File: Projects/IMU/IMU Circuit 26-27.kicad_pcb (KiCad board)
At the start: 2 copper layers, 32.1 x 33.1 mm, 13 parts, among them U1 TJA1050DRG, U2 MCP2515-I, U3 TM171, X1 8MHz

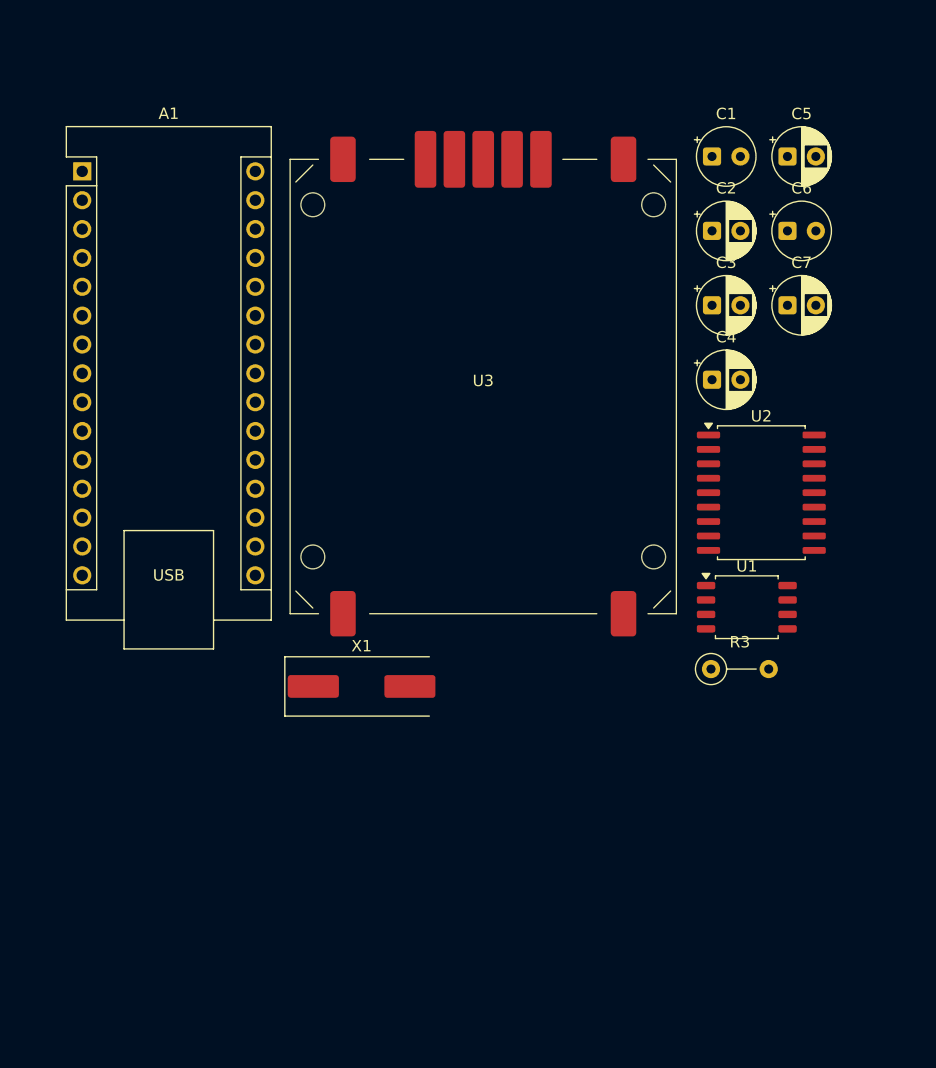
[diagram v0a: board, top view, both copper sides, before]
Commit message: the pcb update
(mostly) done routing, fill areas, and silkscreens
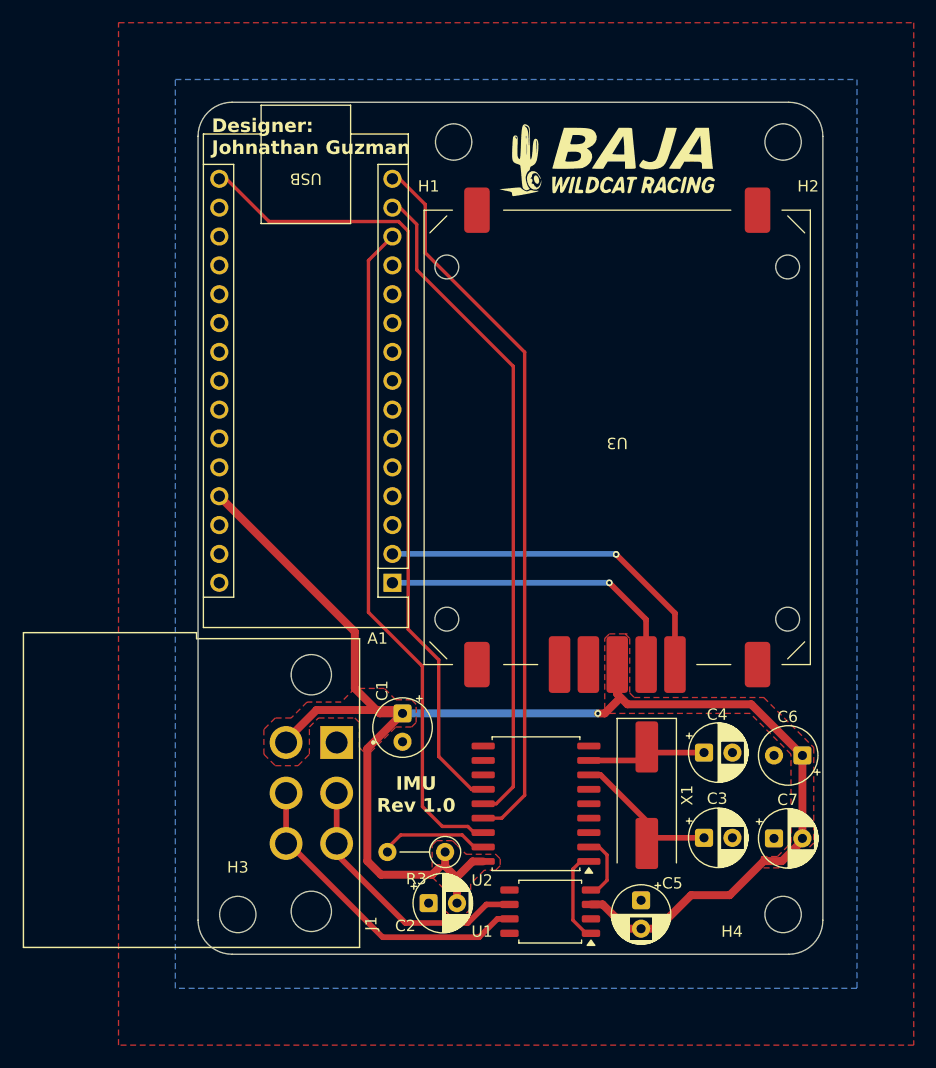
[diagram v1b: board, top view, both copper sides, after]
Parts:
- added G***: LOGO, Baja Logo for PCB:Baja Logo, F.Cu at (138.0, 82.1)
- added G***: LOGO, Baja Logo for PCB:Baja Logo, B.Cu at (138.9, 82.1)
- added H1: MountingHole, MountingHole:MountingHole_3.2mm_M3, F.Cu at (124.5, 80.5)
- added H2: MountingHole, MountingHole:MountingHole_3.2mm_M3, F.Cu at (153.5, 80.5)
- added H3: MountingHole, MountingHole:MountingHole_3.2mm_M3, F.Cu at (105.5, 148.5)
- added H4: MountingHole, MountingHole:MountingHole_3.2mm_M3, F.Cu at (153.5, 148.5)
- added J1: Conn_02x03_Counter_Clockwise, DTF13:TE_DTF13-6P, F.Cu at (112.0, 137.8)
- moved C5 66.7 mm to (141.0, 147.2), turned to -90 degrees
- moved C2 64.2 mm to (122.3, 147.5)
- moved C1 56.1 mm to (120.0, 130.8), turned to -90 degrees
- moved C7 46.9 mm to (152.7, 141.8)
- moved C3 46.9 mm to (146.5, 141.8)
- moved C6 46.2 mm to (155.2, 134.5), turned to 180 degrees
- moved A1 45.4 mm to (119.1, 119.3), turned to 180 degrees
- moved U2 33.8 mm to (131.8, 138.8), turned to 180 degrees
- moved C4 32.8 mm to (146.5, 134.2)
- moved U1 31.9 mm to (133.0, 148.2), turned to 180 degrees
- moved R3 28.4 mm to (123.8, 143.0), turned to 180 degrees
- moved X1 26.9 mm to (141.5, 138.0), turned to -90 degrees
- moved U3 12.6 mm to (138.9, 106.5), turned to 180 degrees
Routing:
- net +5V: track 0.00 -> 138.6 mm, vias 0 -> 2
- net SCK: track 0.00 -> 71.0 mm
- net SO: track 0.00 -> 63.9 mm
- net CS: track 0.00 -> 59.3 mm
- net SI: track 0.00 -> 59.0 mm
- net Net-(A1-D0/RX): track 0.00 -> 31.4 mm, vias 0 -> 1
- net High: track 0.00 -> 28.2 mm
- net Net-(A1-D1/TX): track 0.00 -> 27.5 mm, vias 0 -> 1
- net Low: track 0.00 -> 23.8 mm
- net Net-(U2-OSC2): track 0.00 -> 14.0 mm
- net Net-(U2-OSC1): track 0.00 -> 11.1 mm
- net Net-(U2-~{RESET}): track 0.00 -> 9.69 mm
- net Net-(U1-TXD): track 0.00 -> 8.24 mm
- net Net-(U1-RXD): track 0.00 -> 5.90 mm
- added copper zone on F.Cu, net +5V
- added copper zone on B.Cu, net 0
- added copper zone on F.Cu, net 0
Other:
- board size 32.1 x 33.1 mm -> 55 x 75 mm
- board text added: "Designer: Johnathan Guzman"
- board text added: "IMU Board Rev 1.0 10/04/26"
- board text added: "IMU Rev 1.0"

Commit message: arduino 3d model added
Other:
- board text added: "Johnathan Guzman Designer ↑ ↑ ↑"
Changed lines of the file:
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@@
 		)
 		(embedded_fonts no)
-		(model "${KICAD10_3DMODEL_DIR}/Module.3dshapes/Arduino_Nano_WithMountingHoles.step"
+		(model "${KICAD10_3DMODEL_DIR}/Module.3dshapes/Arduino_NANO_CH340.step"
 			(offset
-				(xyz 0 0 0)
+				(xyz 7.6 -17.8 4)
 			)
 			(scale
@@
 			)
 			(rotate
-				(xyz 0 0 0)
+				(xyz -0 -0 -90)
 			)
 		)
@@
 		(layer "Edge.Cuts")
 	)
-	(gr_text "Designer:\nJohnathan Guzman"
+	(gr_text "Johnathan Guzman\nDesigner ↑ ↑ ↑"
 		(at 103.2 81.7 0)
 		(layer "F.SilkS" knockout)
@@
 	)
 	(segment
-		(start 120.5 123.4)
-		(end 120.5 88.343654)
-		(width 0.3)
-		(layer "F.Cu")
-		(net "SCK")
-	)
-	(segment
-		(start 108.25 87.5)
+		(start 108.3 87.55)
 		(end 104.49 83.74)
 		(width 0.3)
@@
 	)
 	(segment
-		(start 119.656346 87.5)
-		(end 108.25 87.5)
+		(start 123.185836 134.590835)
+		(end 123.185836 126.085836)
 		(width 0.3)
 		(layer "F.Cu")
@@
 	)
 	(segment
-		(start 123.185836 126.085836)
-		(end 120.5 123.4)
+		(start 127.1 137.48)
+		(end 126.075001 137.48)
 		(width 0.3)
 		(layer "F.Cu")
@@
 	)
 	(segment
-		(start 127.1 137.48)
-		(end 126.075001 137.48)
+		(start 119.706346 87.55)
+		(end 108.3 87.55)
 		(width 0.3)
 		(layer "F.Cu")
@@
 	)
 	(segment
-		(start 120.5 88.343654)
-		(end 119.656346 87.5)
+		(start 123.185836 126.085836)
+		(end 120.5 123.4)
 		(width 0.3)
 		(layer "F.Cu")
@@
 	)
 	(segment
-		(start 123.185836 134.590835)
-		(end 123.185836 126.085836)
+		(start 120.5 123.4)
+		(end 120.5 88.343654)
 		(width 0.3)
 		(layer "F.Cu")
@@
 		(width 0.3)
 		(layer "F.Cu")
+		(net "SCK")
+	)
+	(segment
+		(start 120.5 88.343654)
+		(end 119.706346 87.55)
+		(width 0.3)
+		(layer "F.Cu")
